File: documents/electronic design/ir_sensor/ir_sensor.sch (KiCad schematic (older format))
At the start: 8 parts, among them U1 TL1838, U3 MPU6050_module, U4 SE8R01_module

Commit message: make double sided pcb for beamer
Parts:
- removed U?: STM32F103HEADER, symbol STM32F103HEADER
- added U?: STM32F103HEADER, symbol STM32F103HEADER
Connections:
- net +3V3: now also U?.20 (+3V3)
- net AD0: now also U?.34 (A2)
- net GND: now also U?.19 (GND)
- net I2C_SCL: now also U?.16 (B8)
- net I2C_SDA: now also U?.17 (B9)
- net IR_RCV: now also U?.5 (A8)
- net MPU5060_INT: now also U?.35 (A1)
- net SE8R01_CE: now also U?.7 (A10)
- net SE8R01_CSN: now also U?.8 (A11)
- net SE8R01_IRQ: now also U?.28 (B0)
- net SPI_MISO: now also U?.29 (A7)
- net SPI_MOSI: now also U?.30 (A6)
- net SPI_SCK: now also U?.31 (A5)
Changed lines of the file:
@@
 EESchema Schematic File Version 2
+LIBS:ir_sensor-rescue
 LIBS:power
 LIBS:device
@@
 $Comp
 L STM32F103HEADER U?
-U 1 1 578E6D6B
+U 1 1 578FE591
 P 1350 2750
 F 0 "U?" H 1500 4000 60  0000 C CNN

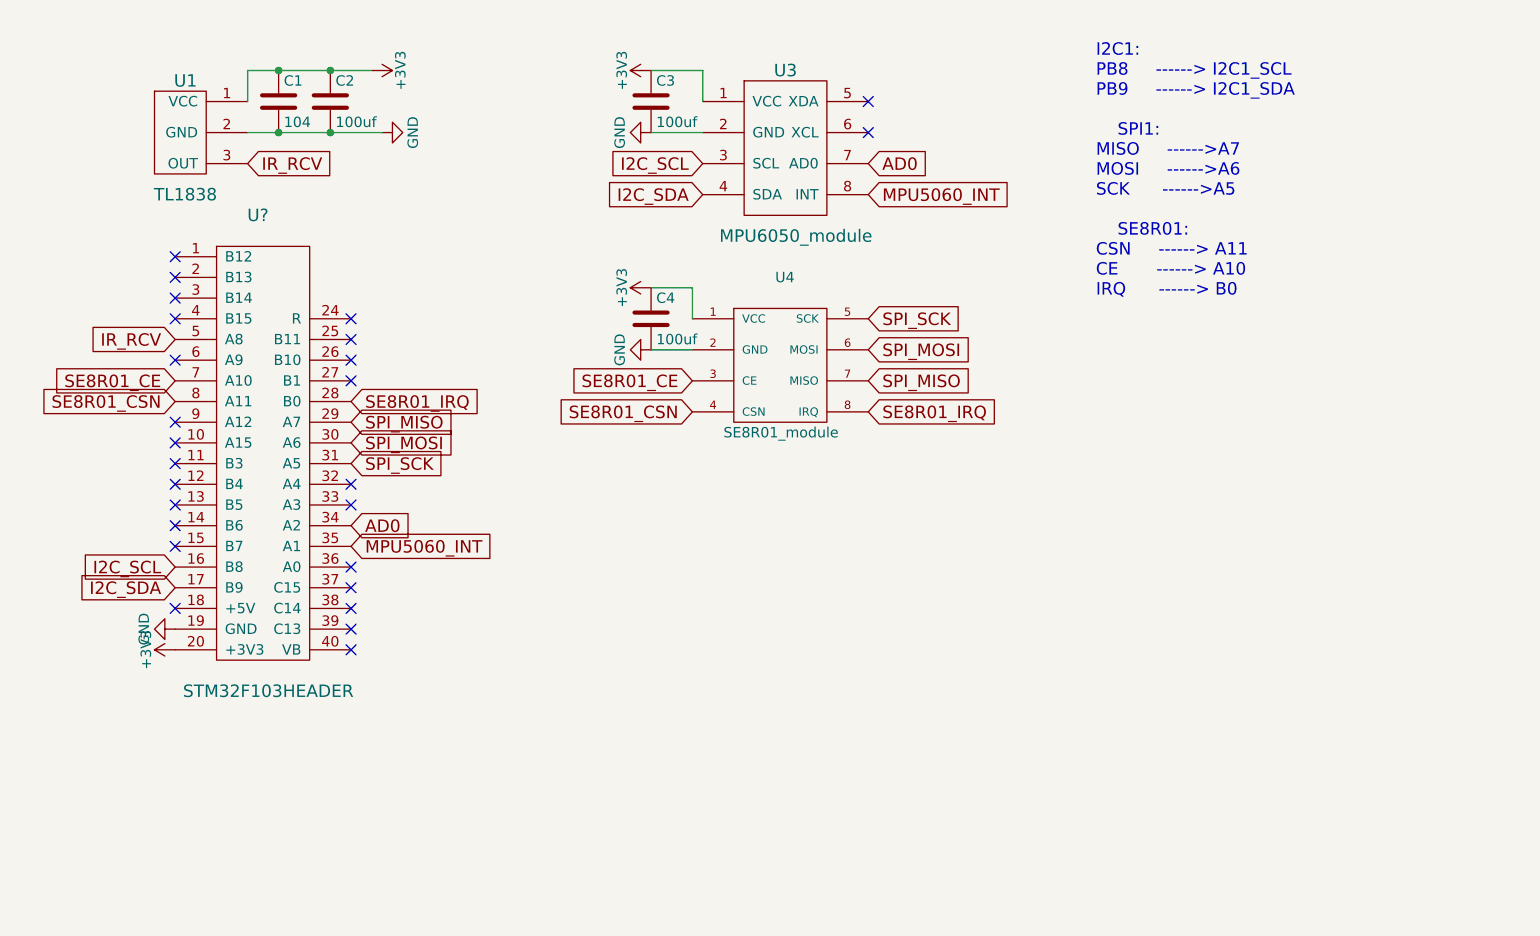
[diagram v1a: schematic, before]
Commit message: make double-sided PCB for beamer; make pcb for receiver
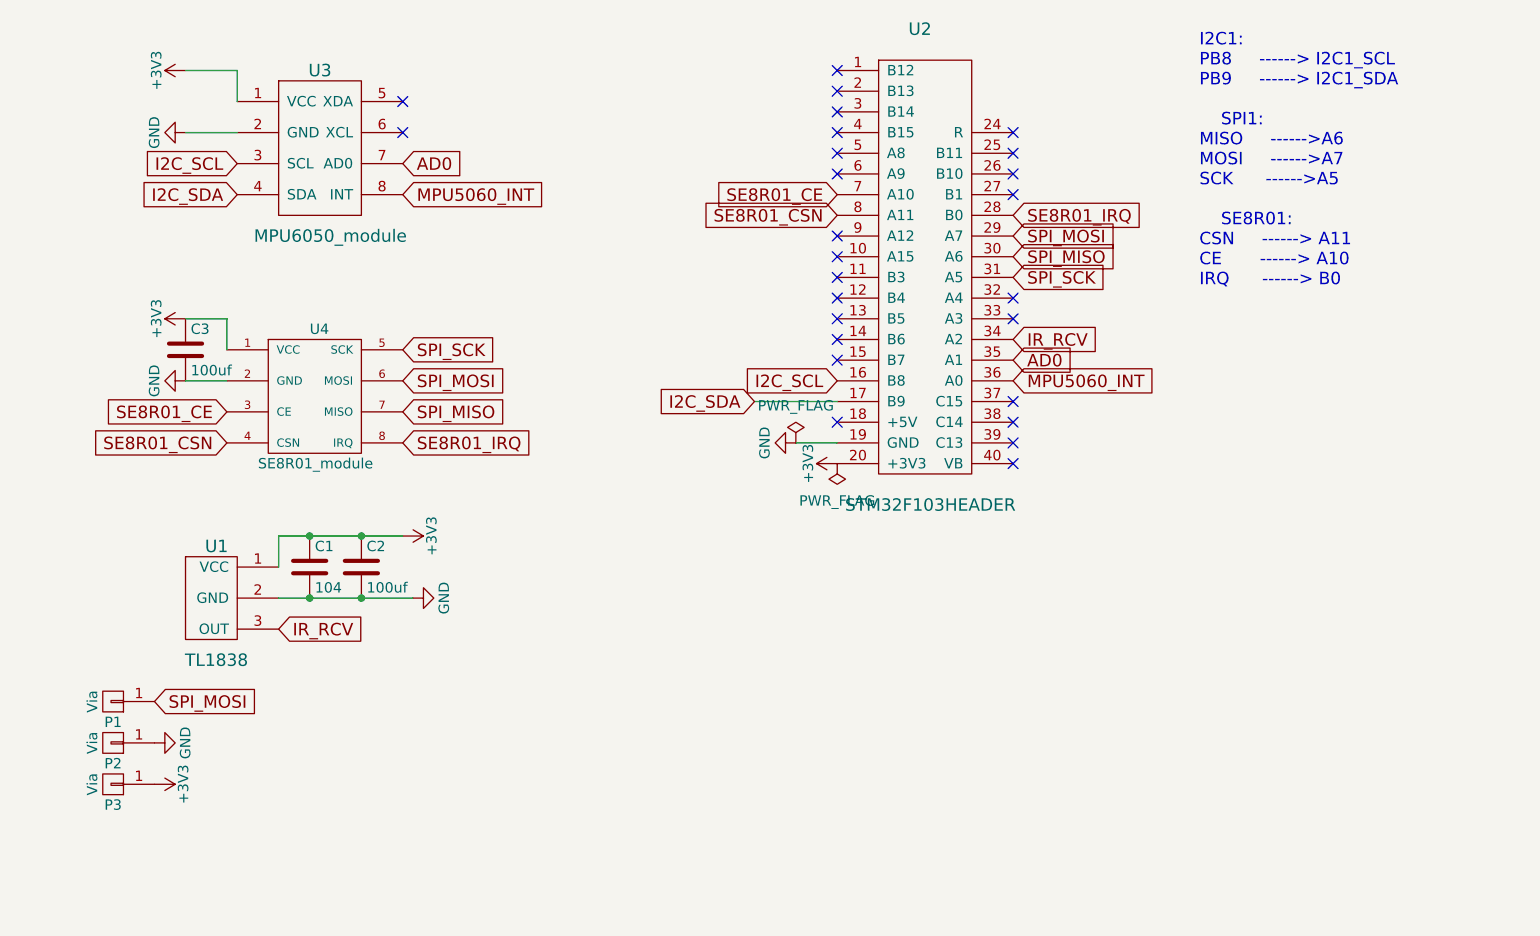
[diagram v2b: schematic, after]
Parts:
- removed C4: 100uf, Capacitors_SMD:C_1206_HandSoldering, symbol C
- removed U?: STM32F103HEADER, symbol STM32F103HEADER
- added P1, P2, P3: Via, footprints:Via, symbol Via
- added U2: STM32F103HEADER, footprints:STM32F103_header_footprint, symbol STM32F103HEADER
- U4: footprint footprints:SE8R01 -> footprints:SE8R01_SMD
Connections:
- net +3V3: now also P3.1 (P1), U2.20 (+3V3)
- net AD0: now also U2.35 (A1)
- net GND: now also P2.1 (P1), U2.19 (GND)
- net I2C_SCL: now also U2.16 (B8)
- net I2C_SDA: now also U2.17 (B9)
- net IR_RCV: now also U2.34 (A2)
- net MPU5060_INT: now also U2.36 (A0)
- net SE8R01_CE: now also U2.7 (A10)
- net SE8R01_CSN: now also U2.8 (A11)
- net SE8R01_IRQ: now also U2.28 (B0)
- net SPI_MISO: now also U2.30 (A6)
- net SPI_MOSI: now also P1.1 (P1), U2.29 (A7)
- net SPI_SCK: now also U2.31 (A5)
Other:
- note added: "I2C1:\nPB8 ------> I2C1_SCL\nPB9 ------> I2C1_SDA\n\n SPI1:\nMISO ------>A6\nMOSI ------>A7\nSCK ------>A5\n\n SE8R01:\nCSN ------> A11\nCE ------> A10\nIRQ ------> B0"
- note removed: "I2C1:\nPB8 ------> I2C1_SCL\nPB9 ------> I2C1_SDA\n\n SPI1:\nMISO ------>A7\nMOSI ------>A6\nSCK ------>A5\n\n SE8R01:\nCSN ------> A11\nCE ------> A10\nIRQ ------> B0"
- moved on the sheet: C1, C2, C3, U1, U3, U4

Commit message: update PCB projects for beamer and sensor
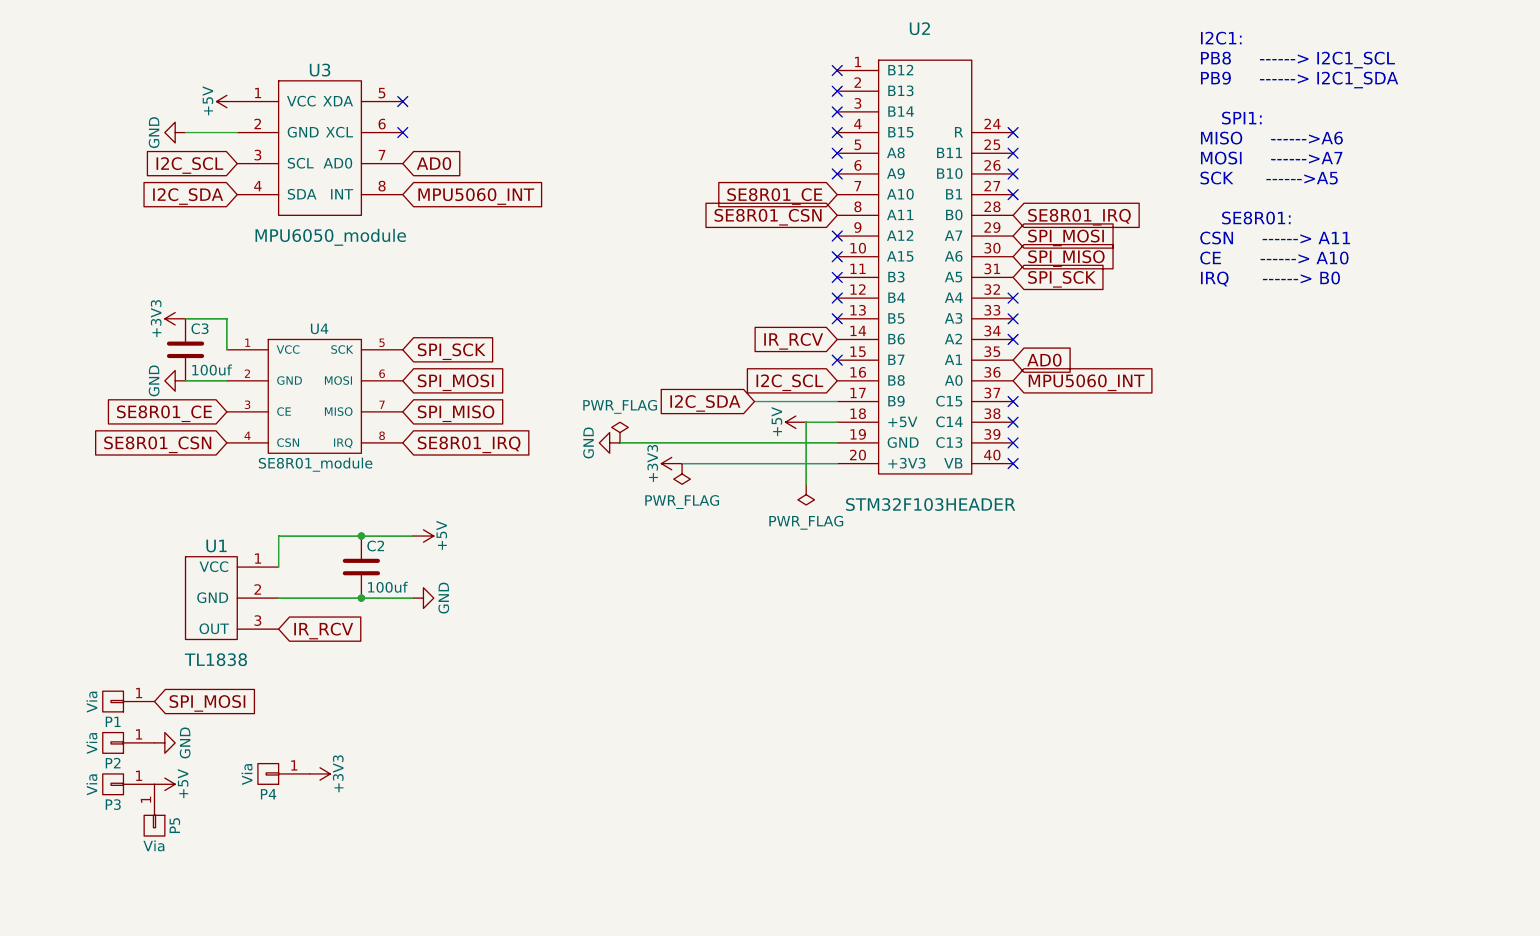
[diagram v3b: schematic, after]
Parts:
- removed C1: 104, Capacitors_SMD:C_1206_HandSoldering, symbol C
- added P4, P5: Via, footprints:Via, symbol Via
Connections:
- net +3V3: now also P4.1 (P1); no longer C2.1, P3.1 (P1), U1.1 (VCC), U3.1 (VCC)
- net IR_RCV: now also U2.14 (B6); no longer U2.34 (A2)
- net +5V: now reaches U2.18 (+5V)
- net +5V: now also C2.1, P3.1 (P1), U1.1 (VCC), U3.1 (VCC), P5.1 (P1)
- no-connect marks 26 -> 25
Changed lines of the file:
@@
 $EndDescr
 $Comp
-L C C1
-U 1 1 578E28E6
-P 1750 3200
-F 0 "C1" H 1775 3300 50  0000 L CNN
-F 1 "104" H 1775 3100 50  0000 L CNN
-F 2 "Capacitors_SMD:C_1206_HandSoldering" H 1788 3050 50  0001 C CNN
-F 3 "" H 1750 3200 50  0000 C CNN
-	1    1750 3200
-	1    0    0    -1
-$EndComp
-Connection ~ 1750 3050
-Wire Wire Line
-	1600 3350 2250 3350
-Connection ~ 1750 3350
-Connection ~ 2000 3050
-$Comp
-L +3V3 #PWR01
-U 1 1 578E2CEF
-P 2200 3050
-F 0 "#PWR01" H 2200 2900 50  0001 C CNN
-F 1 "+3V3" H 2200 3190 50  0000 C CNN
-F 2 "" H 2200 3050 50  0000 C CNN
-F 3 "" H 2200 3050 50  0000 C CNN
-	1    2200 3050
-	0    1    1    0
-$EndComp
-$Comp
-L GND #PWR02
+L GND #PWR01
 U 1 1 578E2D11
 P 2250 3350
-F 0 "#PWR02" H 2250 3100 50  0001 C CNN
+F 0 "#PWR01" H 2250 3100 50  0001 C CNN
 F 1 "GND" H 2250 3200 50  0000 C CNN
 F 2 "" H 2250 3350 50  0000 C CNN
@@
 	0    -1   -1   0
 $EndComp
-Connection ~ 2000 3350
-$Comp
-L +3V3 #PWR03
-U 1 1 578E38B9
-P 1150 800
-F 0 "#PWR03" H 1150 650 50  0001 C CNN
-F 1 "+3V3" H 1150 940 50  0000 C CNN
-F 2 "" H 1150 800 50  0000 C CNN
-F 3 "" H 1150 800 50  0000 C CNN
-	1    1150 800
-	0    -1   -1   0
-$EndComp
-$Comp
-L GND #PWR04
+$Comp
+L GND #PWR02
 U 1 1 578E393C
 P 1150 1100
-F 0 "#PWR04" H 1150 850 50  0001 C CNN
+F 0 "#PWR02" H 1150 850 50  0001 C CNN
 F 1 "GND" H 1150 950 50  0000 C CNN
 F 2 "" H 1150 1100 50  0000 C CNN
@@
 Wire Wire Line
 	1400 1100 1150 1100
-Wire Wire Line
-	1400 950  1400 800
-Wire Wire Line
-	1400 800  1150 800
 Text GLabel 4300 2300 0    60   Input ~ 0
 I2C_SCL
@@
 	1350 2000 1150 2000
 $Comp
-L +3V3 #PWR05
+L +3V3 #PWR03
 U 1 1 578E7909
 P 1150 2000
-F 0 "#PWR05" H 1150 1850 50  0001 C CNN
+F 0 "#PWR03" H 1150 1850 50  0001 C CNN
 F 1 "+3V3" H 1150 2140 50  0000 C CNN
 F 2 "" H 1150 2000 50  0000 C CNN
@@
 $EndComp
 $Comp
-L GND #PWR06
+L GND #PWR04
 U 1 1 578E792F
 P 1150 2300
-F 0 "#PWR06" H 1150 2050 50  0001 C CNN
+F 0 "#PWR04" H 1150 2050 50  0001 C CNN
 F 1 "GND" H 1150 2150 50  0000 C CNN
 F 2 "" H 1150 2300 50  0000 C CNN
@@
 Text GLabel 1600 3500 2    60   Input ~ 0
 IR_RCV
-Text GLabel 5150 2100 2    60   Input ~ 0
+Text GLabel 4300 2100 0    60   Input ~ 0
 IR_RCV
 NoConn ~ 4300 800
@@
 NoConn ~ 4300 1900
 NoConn ~ 4300 2000
-NoConn ~ 4300 2500
 NoConn ~ 5150 2700
 NoConn ~ 5150 2600
@@
 NoConn ~ 5150 2400
 NoConn ~ 4300 2200
-NoConn ~ 4300 2100
+NoConn ~ 5150 2100
 NoConn ~ 5150 2000
 NoConn ~ 5150 1900
@@
 NoConn ~ 5150 1100
 $Comp
-L +3V3 #PWR07
+L +3V3 #PWR05
 U 1 1 578E9CFC
-P 4300 2700
-F 0 "#PWR07" H 4300 2550 50  0001 C CNN
-F 1 "+3V3" H 4300 2840 50  0000 C CNN
-F 2 "" H 4300 2700 50  0000 C CNN
-F 3 "" H 4300 2700 50  0000 C CNN
-	1    4300 2700
-	0    -1   -1   0
-$EndComp
-$Comp
-L GND #PWR08
+P 3550 2700
+F 0 "#PWR05" H 3550 2550 50  0001 C CNN
+F 1 "+3V3" H 3550 2840 50  0000 C CNN
+F 2 "" H 3550 2700 50  0000 C CNN
+F 3 "" H 3550 2700 50  0000 C CNN
+	1    3550 2700
+	0    -1   -1   0
+$EndComp
+$Comp
+L GND #PWR06
 U 1 1 578E9D22
-P 4100 2600
-F 0 "#PWR08" H 4100 2350 50  0001 C CNN
-F 1 "GND" H 4100 2450 50  0000 C CNN
-F 2 "" H 4100 2600 50  0000 C CNN
-F 3 "" H 4100 2600 50  0000 C CNN
-	1    4100 2600
+P 3250 2600
+F 0 "#PWR06" H 3250 2350 50  0001 C CNN
+F 1 "GND" H 3250 2450 50  0000 C CNN
+F 2 "" H 3250 2600 50  0000 C CNN
+F 3 "" H 3250 2600 50  0000 C CNN
+	1    3250 2600
 	0    1    1    0
 $EndComp
@@
 	1    0    0    -1
 $EndComp
-Wire Wire Line
-	1600 3200 1600 3050
-Wire Wire Line
-	1600 3050 2200 3050
 $Comp
 L TL1838 U1
@@
 $EndComp
 $Comp
-L STM32F103HEADER U2
-U 1 1 57911877
-P 4550 1850
-F 0 "U2" H 4700 3100 60  0000 C CNN
-F 1 "STM32F103HEADER" H 4750 800 60  0000 C CNN
-F 2 "footprints:STM32F103_header_footprint" H 3900 2850 60  0001 C CNN
-F 3 "" H 3900 2850 60  0000 C CNN
-	1    4550 1850
-	1    0    0    -1
-$EndComp
-$Comp
 L Via P1
 U 1 1 57913A3B
@@
 $EndComp
 $Comp
-L PWR_FLAG #FLG09
+L PWR_FLAG #FLG07
 U 1 1 57913BE4
-P 4100 2600
-F 0 "#FLG09" H 4100 2695 50  0001 C CNN
-F 1 "PWR_FLAG" H 4100 2780 50  0000 C CNN
-F 2 "" H 4100 2600 50  0000 C CNN
-F 3 "" H 4100 2600 50  0000 C CNN
-	1    4100 2600
-	1    0    0    -1
-$EndComp
-$Comp
-L PWR_FLAG #FLG010
+P 3250 2600
+F 0 "#FLG07" H 3250 2695 50  0001 C CNN
+F 1 "PWR_FLAG" H 3250 2780 50  0000 C CNN
+F 2 "" H 3250 2600 50  0000 C CNN
+F 3 "" H 3250 2600 50  0000 C CNN
+	1    3250 2600
+	1    0    0    -1
+$EndComp
+$Comp
+L PWR_FLAG #FLG08
 U 1 1 57913C36
-P 4300 2700
-F 0 "#FLG010" H 4300 2795 50  0001 C CNN
-F 1 "PWR_FLAG" H 4300 2880 50  0000 C CNN
-F 2 "" H 4300 2700 50  0000 C CNN
-F 3 "" H 4300 2700 50  0000 C CNN
-	1    4300 2700
-	-1   0    0    1
-$EndComp
-Wire Wire Line
-	4100 2600 4300 2600
+P 3550 2700
+F 0 "#FLG08" H 3550 2795 50  0001 C CNN
+F 1 "PWR_FLAG" H 3550 2880 50  0000 C CNN
+F 2 "" H 3550 2700 50  0000 C CNN
+F 3 "" H 3550 2700 50  0000 C CNN
+	1    3550 2700
+	-1   0    0    1
+$EndComp
 Wire Wire Line
 	4300 2400 3900 2400
@@
 Text GLabel 1000 3850 2    60   Input ~ 0
 SPI_MOSI
-$Comp
-L GND #PWR011
-U 1 1 57915018
-P 1000 4050
-F 0 "#PWR011" H 1000 3800 50  0001 C CNN
-F 1 "GND" H 1000 3900 50  0000 C CNN
-F 2 "" H 1000 4050 50  0000 C CNN
-F 3 "" H 1000 4050 50  0000 C CNN
-	1    1000 4050
-	0    -1   -1   0
-$EndComp
-$Comp
-L +3V3 #PWR012
-U 1 1 5791503E
-P 1000 4250
-F 0 "#PWR012" H 1000 4100 50  0001 C CNN
-F 1 "+3V3" H 1000 4390 50  0000 C CNN
-F 2 "" H 1000 4250 50  0000 C CNN
-F 3 "" H 1000 4250 50  0000 C CNN
-	1    1000 4250
-	0    1    1    0
-$EndComp
-$Comp
-L Via P2
-U 1 1 57915064
-P 800 4050
-F 0 "P2" H 800 4150 50  0000 C CNN
-F 1 "Via" V 900 4050 50  0000 C CNN
-F 2 "footprints:Via" H 800 4050 50  0001 C CNN
-F 3 "" H 800 4050 50  0000 C CNN
-	1    800  4050
-	-1   0    0    1
-$EndComp
 $Comp
 L Via P3
@@
 	-1   0    0    1
 $EndComp
+$Comp
+L +5V #PWR09
+U 1 1 5791DCDE
+P 4150 2500
+F 0 "#PWR09" H 4150 2350 50  0001 C CNN
+F 1 "+5V" H 4150 2640 50  0000 C CNN
+F 2 "" H 4150 2500 50  0000 C CNN
+F 3 "" H 4150 2500 50  0000 C CNN
+	1    4150 2500
+	0    -1   -1   0
+$EndComp
+$Comp
+L +5V #PWR010
+U 1 1 5791DD0E
+P 1400 950
+F 0 "#PWR010" H 1400 800 50  0001 C CNN
+F 1 "+5V" H 1400 1090 50  0000 C CNN
+F 2 "" H 1400 950 50  0000 C CNN
+F 3 "" H 1400 950 50  0000 C CNN
+	1    1400 950
+	0    -1   -1   0
+$EndComp
+$Comp
+L +5V #PWR011
+U 1 1 5791E3D7
+P 2250 3050
+F 0 "#PWR011" H 2250 2900 50  0001 C CNN
+F 1 "+5V" H 2250 3190 50  0000 C CNN
+F 2 "" H 2250 3050 50  0000 C CNN
+F 3 "" H 2250 3050 50  0000 C CNN
+	1    2250 3050
+	0    1    1    0
+$EndComp
+$Comp
+L +5V #PWR012
+U 1 1 5791E96E
+P 1000 4250
+F 0 "#PWR012" H 1000 4100 50  0001 C CNN
+F 1 "+5V" H 1000 4390 50  0000 C CNN
+F 2 "" H 1000 4250 50  0000 C CNN
+F 3 "" H 1000 4250 50  0000 C CNN
+	1    1000 4250
+	0    1    1    0
+$EndComp
+Wire Wire Line
+	4300 2700 3550 2700
+Wire Wire Line
+	4300 2600 3250 2600
+Wire Wire Line
+	1600 3050 2250 3050
+Connection ~ 2000 3050
+Wire Wire Line
+	1600 3050 1600 3200
+Wire Wire Line
+	1600 3350 2250 3350
+Connection ~ 2000 3350
+$Comp
+L Via P2
+U 1 1 5791FA8C
+P 800 4050
+F 0 "P2" H 800 4150 50  0000 C CNN
+F 1 "Via" V 900 4050 50  0000 C CNN
+F 2 "footprints:Via" H 800 4050 50  0001 C CNN
+F 3 "" H 800 4050 50  0000 C CNN
+	1    800  4050
+	-1   0    0    1
+$EndComp
+$Comp
+L GND #PWR013
+U 1 1 5791FABF
+P 1000 4050
+F 0 "#PWR013" H 1000 3800 50  0001 C CNN
+F 1 "GND" H 1000 3900 50  0000 C CNN
+F 2 "" H 1000 4050 50  0000 C CNN
+F 3 "" H 1000 4050 50  0000 C CNN
+	1    1000 4050
+	0    -1   -1   0
+$EndComp
+$Comp
+L STM32F103HEADER U2
+U 1 1 5795C959
+P 4550 1850
+F 0 "U2" H 4700 3100 60  0000 C CNN
+F 1 "STM32F103HEADER" H 4750 800 60  0000 C CNN
+F 2 "footprints:STM32F103_header_footprint" H 3900 2850 60  0001 C CNN
+F 3 "" H 3900 2850 60  0000 C CNN
+	1    4550 1850
+	1    0    0    -1
+$EndComp
+$Comp
+L PWR_FLAG #FLG014
+U 1 1 5795CABB
+P 4150 2800
+F 0 "#FLG014" H 4150 2895 50  0001 C CNN
+F 1 "PWR_FLAG" H 4150 2980 50  0000 C CNN
+F 2 "" H 4150 2800 50  0000 C CNN
+F 3 "" H 4150 2800 50  0000 C CNN
+	1    4150 2800
+	-1   0    0    1
+$EndComp
+Wire Wire Line
+	4150 2800 4150 2500
+Wire Wire Line
+	4150 2500 4300 2500
+$Comp
+L Via P4
+U 1 1 5795CDD1
+P 1550 4200
+F 0 "P4" H 1550 4300 50  0000 C CNN
+F 1 "Via" V 1650 4200 50  0000 C CNN
+F 2 "footprints:Via" H 1550 4200 50  0001 C CNN
+F 3 "" H 1550 4200 50  0000 C CNN
+	1    1550 4200
+	-1   0    0    1
+$EndComp
+$Comp
+L +3V3 #PWR015
+U 1 1 5795CE59
+P 1750 4200
+F 0 "#PWR015" H 1750 4050 50  0001 C CNN
+F 1 "+3V3" H 1750 4340 50  0000 C CNN
+F 2 "" H 1750 4200 50  0000 C CNN
+F 3 "" H 1750 4200 50  0000 C CNN
+	1    1750 4200
+	0    1    1    0
+$EndComp
+$Comp
+L Via P5
+U 1 1 5795D0A9
+P 1000 4450
+F 0 "P5" H 1000 4550 50  0000 C CNN
+F 1 "Via" V 1100 4450 50  0000 C CNN
+F 2 "footprints:Via" H 1000 4450 50  0001 C CNN
+F 3 "" H 1000 4450 50  0000 C CNN
+	1    1000 4450
+	0    1    1    0
+$EndComp
 $EndSCHEMATC
